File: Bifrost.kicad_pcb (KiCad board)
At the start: 4 copper layers, 68.6 x 53.3 mm, 82 parts, among them IC1 DS1085Z-10+, IC2 DS1085Z-10+, J1 OIP, J10 Barrel_Jack_Switch, J5 CalCK, U1 HMC900LP5E, U2 HMC860LP3E

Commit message: Rounded tracks
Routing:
- net GND: vias 6 -> 15

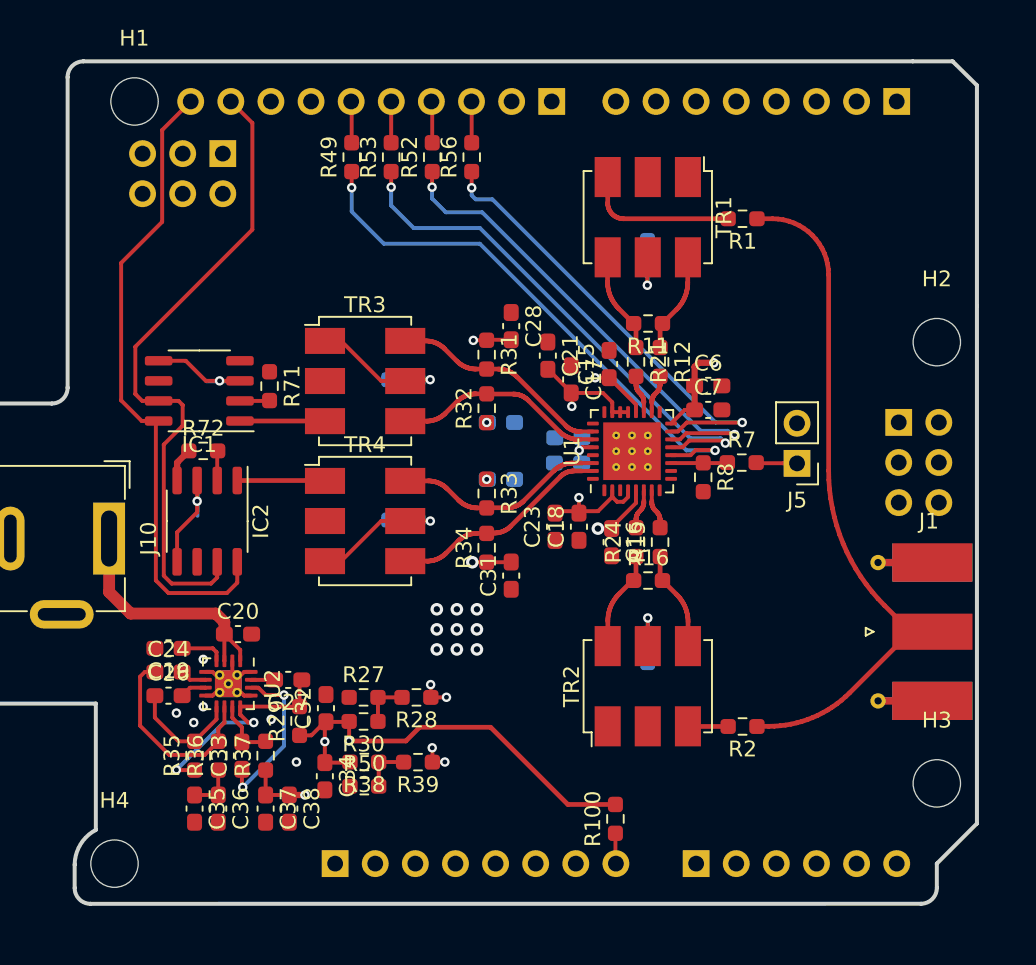
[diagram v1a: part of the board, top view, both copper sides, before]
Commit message: Teardroped
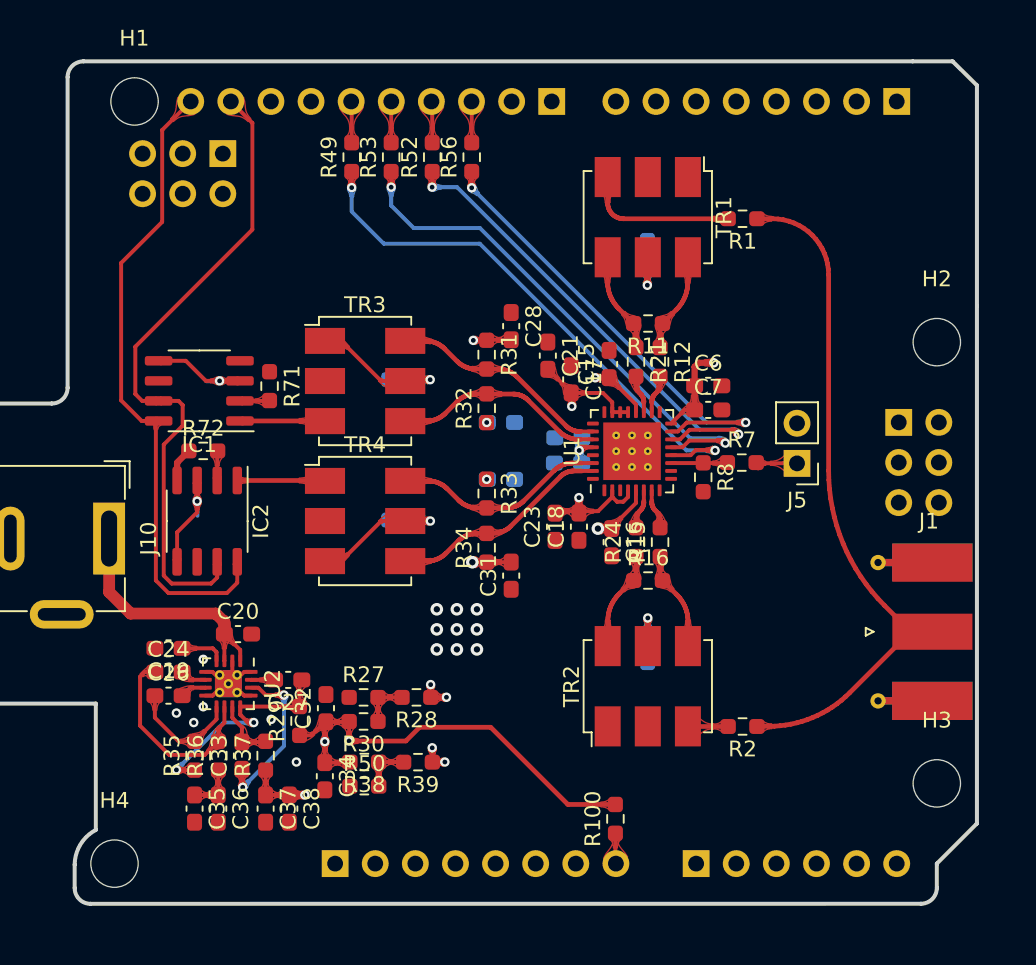
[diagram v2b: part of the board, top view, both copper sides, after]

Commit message: Via fencing
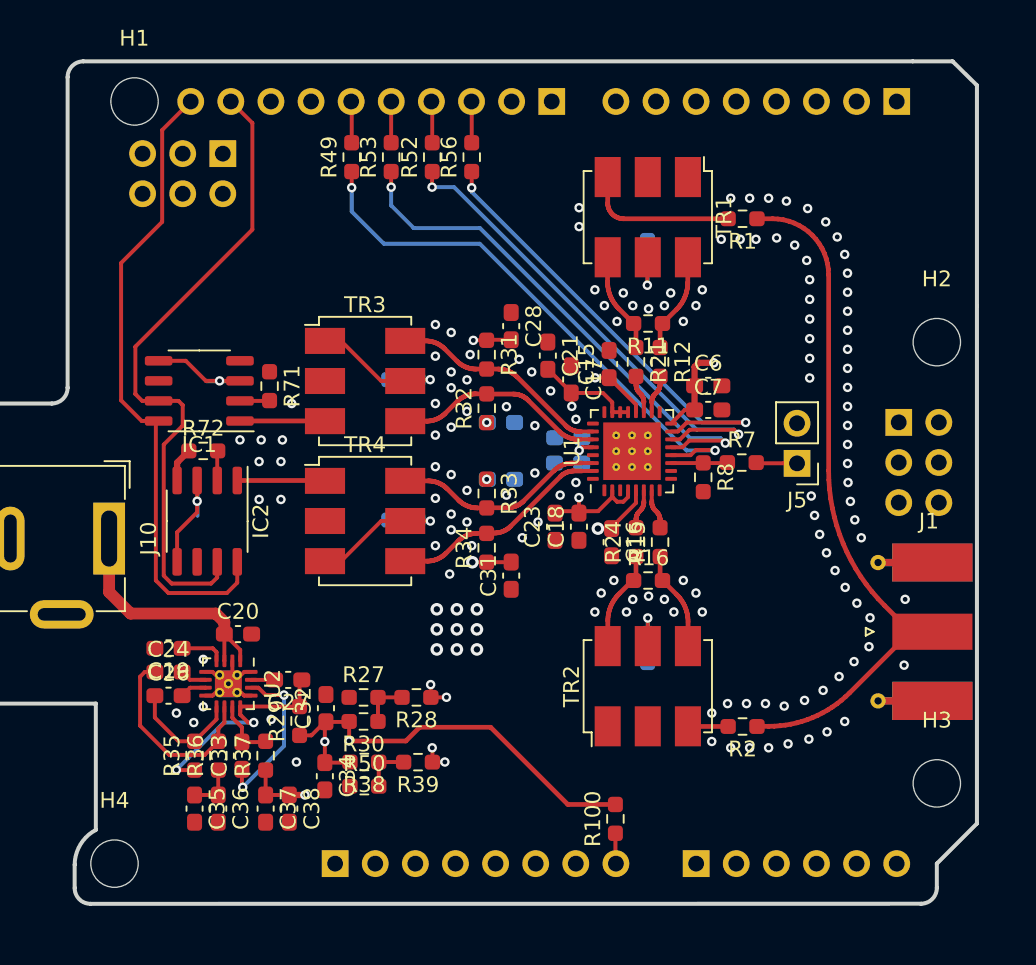
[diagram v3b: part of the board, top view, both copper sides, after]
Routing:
- net GND: vias 15 -> 138
- net (no net): vias 0 -> 5

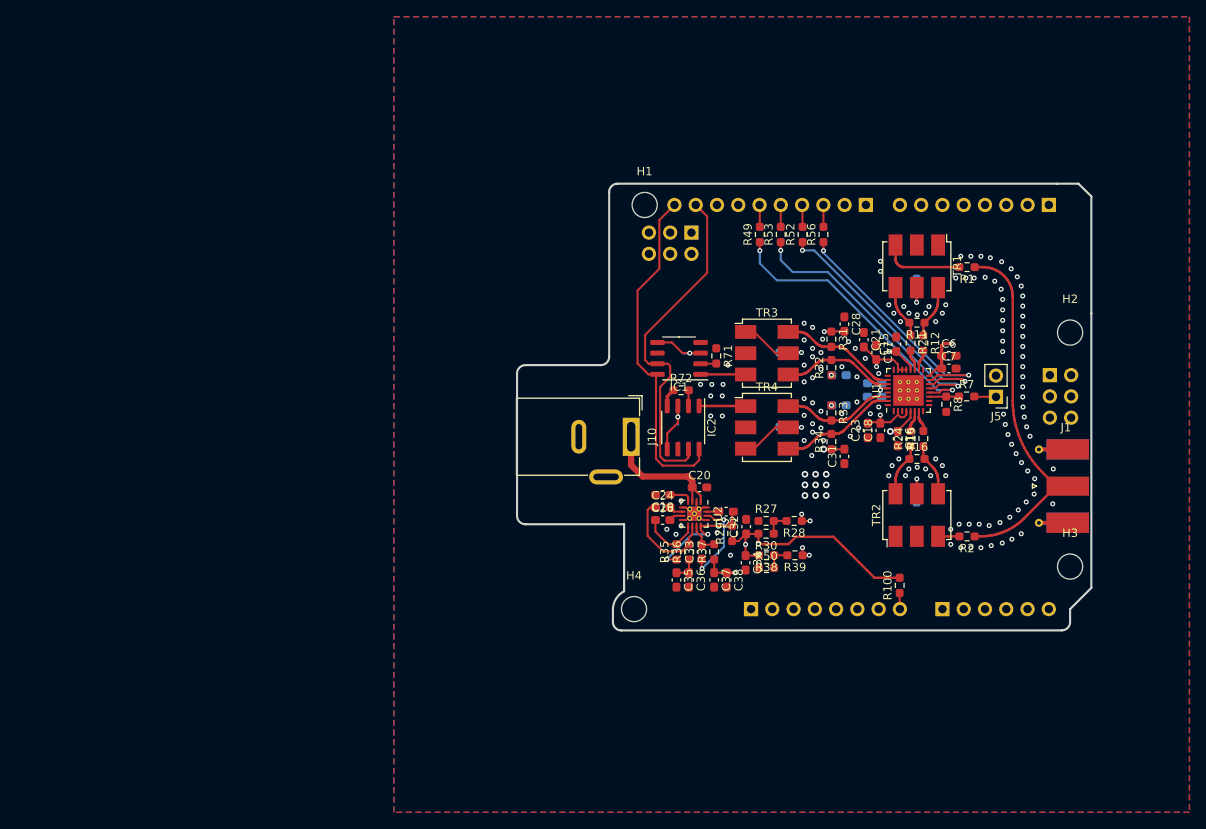
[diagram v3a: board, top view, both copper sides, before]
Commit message: Added Logic gate buffer for the oscillator
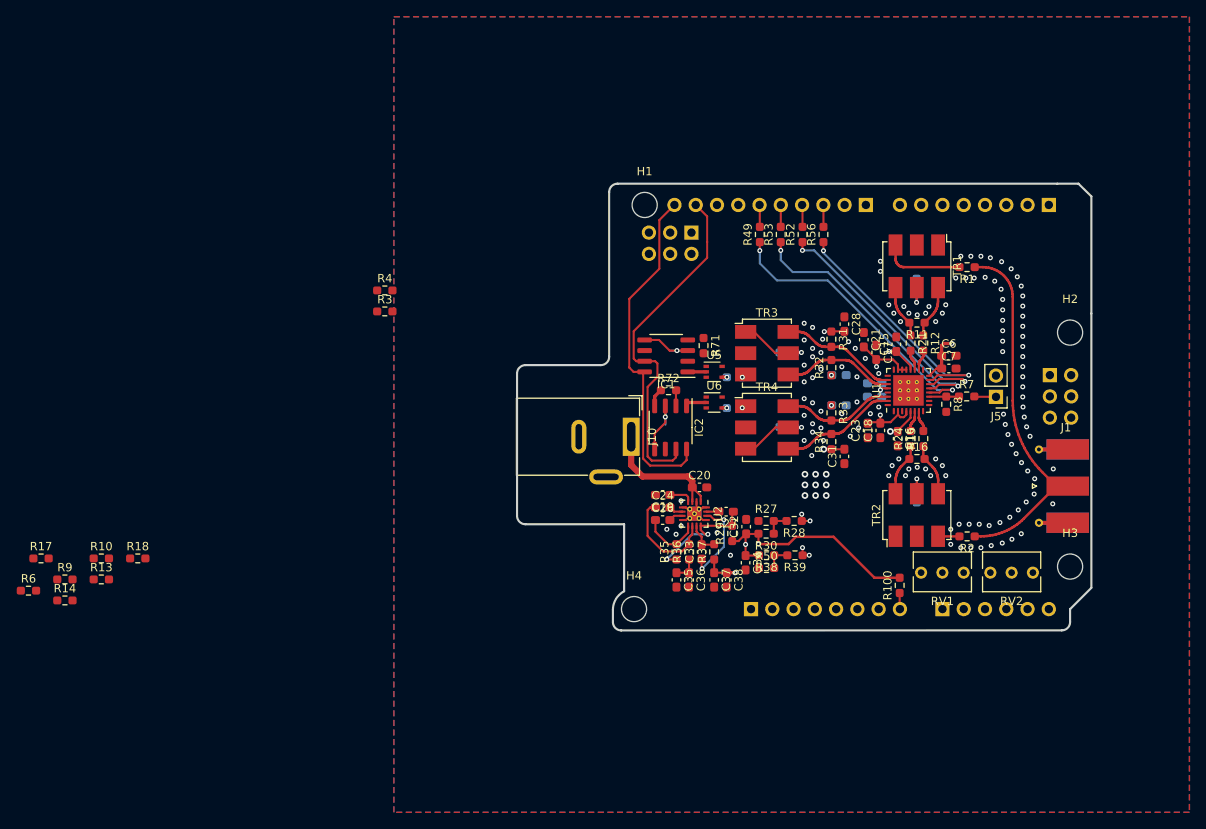
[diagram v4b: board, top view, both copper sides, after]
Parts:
- added R10: 0, Resistor_SMD:R_0603_1608Metric_Pad0.98x0.95mm_HandSolder, F.Cu at (64.6, 123.1)
- added R13: 0, Resistor_SMD:R_0603_1608Metric_Pad0.98x0.95mm_HandSolder, F.Cu at (64.6, 125.6)
- added R14: 0, Resistor_SMD:R_0603_1608Metric_Pad0.98x0.95mm_HandSolder, F.Cu at (60.2, 128.1)
- added R17: 0, Resistor_SMD:R_0603_1608Metric_Pad0.98x0.95mm_HandSolder, F.Cu at (57.4, 123.1)
- added R18: 0, Resistor_SMD:R_0603_1608Metric_Pad0.98x0.95mm_HandSolder, F.Cu at (68.9, 123.1)
- added R19: 0, Resistor_SMD:R_0603_1608Metric_Pad0.98x0.95mm_HandSolder, B.Cu at (140.2, 105.1)
- added R3: 0, Resistor_SMD:R_0603_1608Metric_Pad0.98x0.95mm_HandSolder, F.Cu at (98.4, 93.6)
- added R4: 0, Resistor_SMD:R_0603_1608Metric_Pad0.98x0.95mm_HandSolder, F.Cu at (98.4, 91.1)
- added R5: 0, Resistor_SMD:R_0603_1608Metric_Pad0.98x0.95mm_HandSolder, B.Cu at (140.2, 101.5)
- added R6: 0, Resistor_SMD:R_0603_1608Metric_Pad0.98x0.95mm_HandSolder, F.Cu at (55.9, 126.9)
- added R9: 0, Resistor_SMD:R_0603_1608Metric_Pad0.98x0.95mm_HandSolder, F.Cu at (60.2, 125.6)
- added RV1: POT_Mod_Freq1, Potentiometer_THT:Potentiometer_Bourns_3266Y_Vertical, F.Cu at (162.5, 124.8)
- added RV2: POT_Mod_Freq2, Potentiometer_THT:Potentiometer_Bourns_3266Y_Vertical, F.Cu at (170.7, 124.8)
- added U5: 74AHC1G04, Package_TO_SOT_SMD:SOT-353_SC-70-5, F.Cu at (137.8, 100.8)
- added U6: 74AHC1G04, Package_TO_SOT_SMD:SOT-353_SC-70-5, F.Cu at (137.8, 104.5)
- moved R71 1.96 mm to (136.5, 97.7)
- moved IC1 1.56 mm to (132.0, 98.9)
- moved IC2 1.50 mm to (132.6, 107.5)
- moved R72 1.50 mm to (132.3, 103.0)
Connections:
- net VDD renamed VCC
- AD1 pad 1: (no net) -> /AD0
- AD1 pad 2: (no net) -> /AD1
- IC1 pad 1: /Sheet60D21B6D/InI+ -> Net-(IC1-Pad1)
- IC2 pad 1: /Sheet60D21B6D/InQ+ -> Net-(IC2-Pad1)
- ICSP2 pad 2: (no net) -> /+5V_Ard_0
- R1 pad 2: /Sheet60D21B6D/OutI+ -> Net-(R1-Pad2)
- R2 pad 2: /Sheet60D21B6D/OutQ+ -> Net-(R10-Pad1)
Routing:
- net /Sheet60D21B6D/InQ+: track 5.57 -> 0.00 mm, vias 0 -> 1
- net /Sheet60D21B6D/InI+: track 5.39 -> 0.00 mm, vias 0 -> 1
- net Net-(IC2-Pad1): track 0.00 -> 2.34 mm
- net Net-(IC1-Pad1): track 0.00 -> 2.21 mm
- net Net-(IC1-Pad2): track 1.88 -> 0.00 mm
- net Net-(R4-Pad2): track 0.00 -> 0.57 mm, vias 0 -> 1
- net Net-(R13-Pad2): track 0.00 -> 0.56 mm, vias 0 -> 1
- net GND: vias 138 -> 130

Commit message: Added options for the tranfo
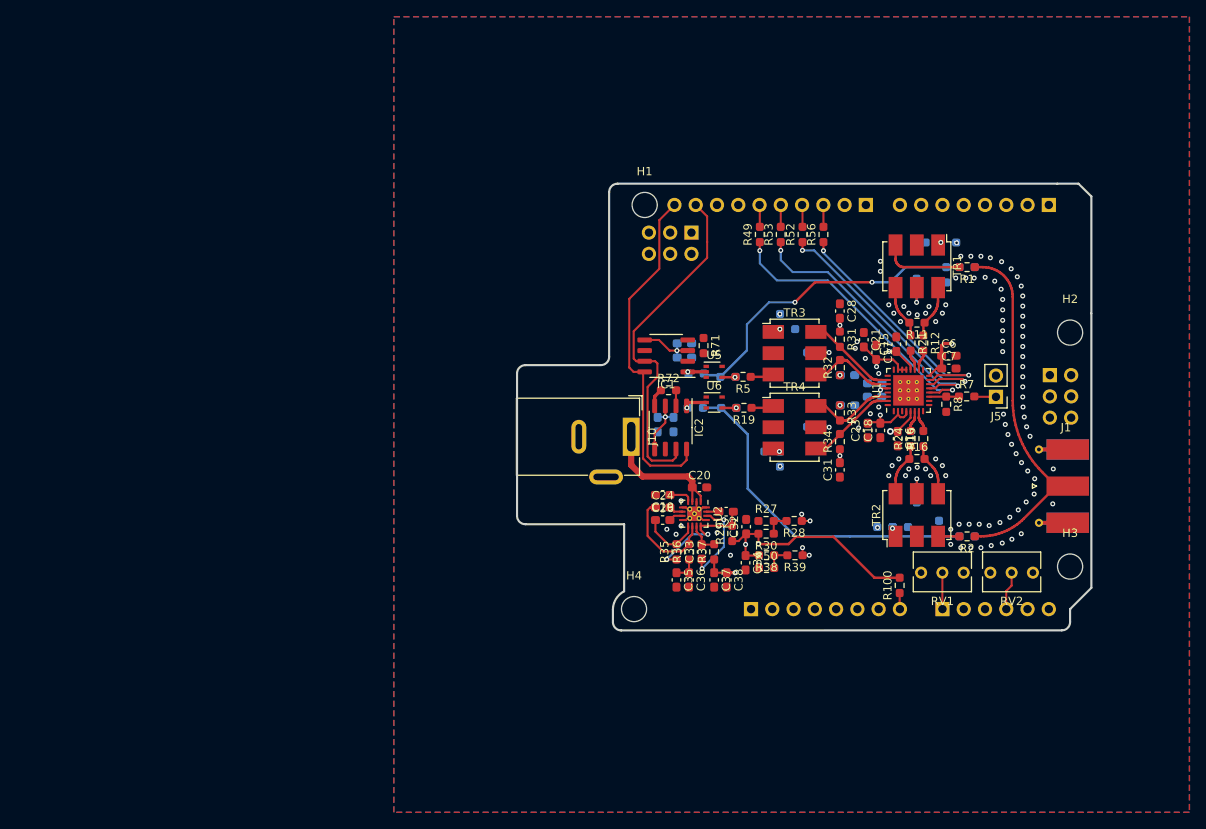
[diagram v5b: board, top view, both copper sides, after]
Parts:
- added C1: 100n, Capacitor_SMD:C_0603_1608Metric_Pad1.08x0.95mm_HandSolder, B.Cu at (134.2, 97.4)
- added C2: 100p, Capacitor_SMD:C_0603_1608Metric_Pad1.08x0.95mm_HandSolder, B.Cu at (134.2, 99.1)
- added C3: 100n, Capacitor_SMD:C_0603_1608Metric_Pad1.08x0.95mm_HandSolder, B.Cu at (132.9, 107.1)
- added C4: 100p, Capacitor_SMD:C_0603_1608Metric_Pad1.08x0.95mm_HandSolder, B.Cu at (131.0, 107.1)
- added R20: 0, Resistor_SMD:R_0603_1608Metric_Pad0.98x0.95mm_HandSolder, B.Cu at (163.9, 85.4)
- added R22: 0, Resistor_SMD:R_0603_1608Metric_Pad0.98x0.95mm_HandSolder, B.Cu at (146.5, 95.7)
- added R23: 0, Resistor_SMD:R_0603_1608Metric_Pad0.98x0.95mm_HandSolder, B.Cu at (145.6, 94.8)
- added R25: 0, Resistor_SMD:R_0603_1608Metric_Pad0.98x0.95mm_HandSolder, B.Cu at (144.7, 110.3)
- added R26: 0, Resistor_SMD:R_0603_1608Metric_Pad0.98x0.95mm_HandSolder, B.Cu at (145.6, 111.2)
- added R40: 0, Resistor_SMD:R_0603_1608Metric_Pad0.98x0.95mm_HandSolder, B.Cu at (158.1, 119.3)
- added R41: 0, Resistor_SMD:R_0603_1608Metric_Pad0.98x0.95mm_HandSolder, B.Cu at (160.0, 119.3)
- R10, R14, R17, R18, R3, R4, R9: moved to B.Cu
- R13, R6: value 0 -> 510; moved to B.Cu
- R19, R5: moved to F.Cu
- moved R6 118.6 mm to (167.9, 88.3)
- moved R9 111.4 mm to (165.5, 89.2), turned to 270 degrees
- moved R18 103.9 mm to (165.7, 85.4)
- moved R13 103.5 mm to (167.9, 120.5), turned to 180 degrees
- moved R10 100.1 mm to (164.6, 119.5), turned to 90 degrees
- moved R17 84.1 mm to (139.5, 105.1)
- moved R14 78.7 mm to (135.5, 105.1), turned to 180 degrees
- moved R4 42.3 mm to (139.4, 101.4)
- moved R3 37.9 mm to (135.6, 101.0), turned to 180 degrees
- moved C46 3.30 mm to (149.8, 107.4)
- moved TR4 3.30 mm to (147.3, 107.4)
- moved C45 3.30 mm to (149.8, 98.5)
- moved TR3 3.30 mm to (147.3, 98.6)
- moved C31 1.70 mm to (152.8, 112.5)
- moved C28 1.65 mm to (152.8, 93.5)
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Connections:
- AD1 pad 2: /AD1 -> (no net)
- AD1 pad 4: (no net) -> /AD3
- R1 pad 2: Net-(R1-Pad2) -> /Sheet60D21B6D/OutI+
- R10 pad 2: /Sheet60D21B6D/OutQ+ -> GND
- R13 pad 1: Net-(R10-Pad1) -> Net-(J1-Pad1)
- R13 pad 2: Net-(R13-Pad2) -> Net-(R10-Pad1)
- R14 pad 1: Net-(R14-Pad1) -> Net-(R10-Pad1)
- R17 pad 1: Net-(R14-Pad1) -> Net-(R10-Pad1)
- R17 pad 2: Net-(R13-Pad2) -> Net-(R17-Pad2)
- R18 pad 1: (no net) -> Net-(R18-Pad1)
- R18 pad 2: (no net) -> CMO
- R19 pad 2: Net-(R13-Pad2) -> Net-(R17-Pad2)
- R2 pad 2: Net-(R10-Pad1) -> /Sheet60D21B6D/OutQ+
- R6 pad 2: Net-(R1-Pad2) -> Net-(J1-Pad1)
- R9 pad 1: Net-(R1-Pad2) -> Net-(R3-Pad1)
- R9 pad 2: /Sheet60D21B6D/OutI+ -> GND
- RV2 pad 2: /AD1 -> /AD3
- TR1 pad 1: GND -> Net-(R18-Pad1)
- TR2 pad 1: GND -> Net-(R40-Pad1)
- TR3 pad 1: CMI -> Net-(R22-Pad2)
- TR4 pad 1: CMI -> Net-(R25-Pad2)
- U6 pad 4: Net-(R13-Pad2) -> Net-(R17-Pad2)
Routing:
- net Net-(R10-Pad1): track 0.00 -> 40.8 mm
- net Net-(R3-Pad1): track 0.00 -> 37.8 mm, vias 0 -> 2
- net CMI: track 23.8 -> 9.81 mm, vias 8 -> 10
- net /AD3: track 0.00 -> 4.62 mm
- net /AD0: track 0.00 -> 4.36 mm
- net /Sheet60D21B6D/IIN: track 13.5 -> 10.4 mm
- net /Sheet60D21B6D/IQN: track 13.5 -> 10.4 mm
- net /Sheet60D21B6D/IIP: track 14.0 -> 10.9 mm
- net /Sheet60D21B6D/IQP: track 14.0 -> 11.0 mm
- net /Sheet60D21B6D/InI+: track 0.00 -> 2.82 mm, vias 1 -> 0
- net /Sheet60D21B6D/InQ+: track 0.00 -> 2.69 mm, vias 1 -> 0
- net Net-(R17-Pad2): track 0.00 -> 1.69 mm, vias 0 -> 1
- net VDDA: track 61.5 -> 60.1 mm
- net Net-(R4-Pad2): track 0.57 -> 1.61 mm
- net Net-(R13-Pad2): track 0.56 -> 0.00 mm, vias 1 -> 0
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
